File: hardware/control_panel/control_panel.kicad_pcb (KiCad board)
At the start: 2 copper layers, 70 x 37 mm, 12 parts

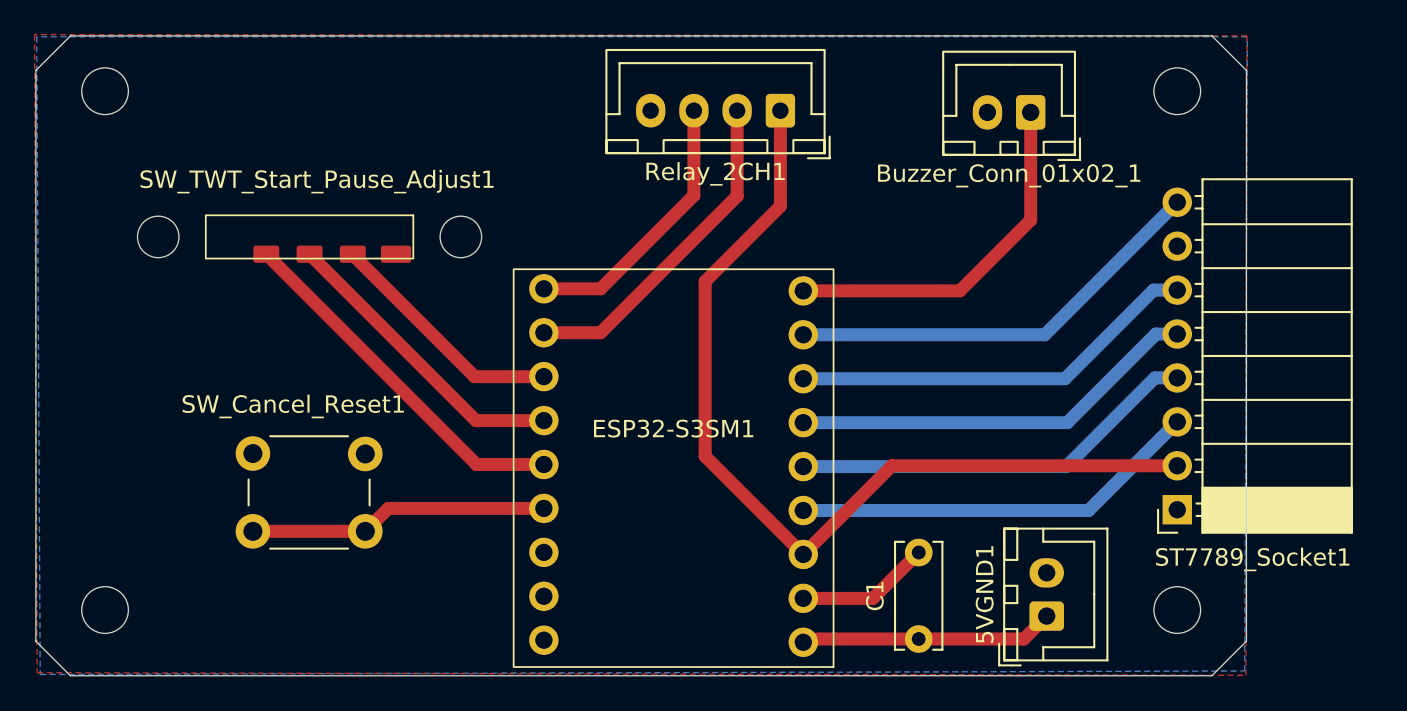
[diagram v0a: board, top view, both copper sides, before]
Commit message: KiCad changes for Control Panel PCB Mountholes
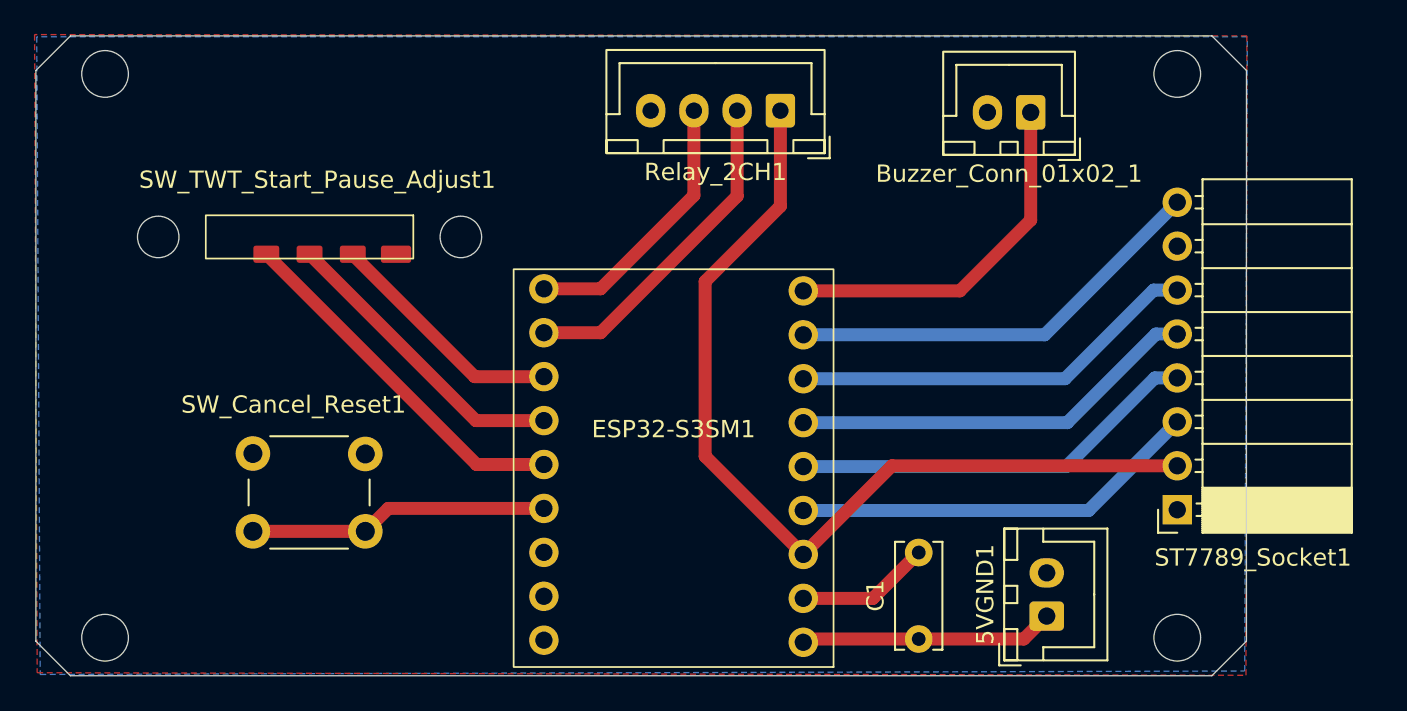
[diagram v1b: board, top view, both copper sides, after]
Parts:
- moved REF** 1.60 mm to (116.0, 84.8)
- moved REF** 1.60 mm to (54.0, 84.8)
- moved REF** 1.00 mm to (54.0, 52.2)
- moved REF** 1.00 mm to (116.0, 52.2)
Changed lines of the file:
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@@
 	(footprint "MountingHole:MountingHole_2.7mm_M2.5_DIN965"
 		(layer "F.Cu")
-		(at 116 83.2)
+		(at 116 84.8)
 		(descr "Mounting Hole 2.7mm, M2.5, no annular, generated by kicad-footprint-generator mountinghole.py")
 		(tags "mountinghole M2.5 DIN965")
@@
 	(footprint "MountingHole:MountingHole_2.7mm_M2.5_DIN965"
 		(layer "F.Cu")
-		(at 54 53.2)
+		(at 54 52.2)
 		(descr "Mounting Hole 2.7mm, M2.5, no annular, generated by kicad-footprint-generator mountinghole.py")
 		(tags "mountinghole M2.5 DIN965")
@@
 	(footprint "MountingHole:MountingHole_2.7mm_M2.5_DIN965"
 		(layer "F.Cu")
-		(at 116 53.2)
+		(at 116 52.2)
 		(descr "Mounting Hole 2.7mm, M2.5, no annular, generated by kicad-footprint-generator mountinghole.py")
 		(tags "mountinghole M2.5 DIN965")
@@
 	(footprint "MountingHole:MountingHole_2.7mm_M2.5_DIN965"
 		(layer "F.Cu")
-		(at 54 83.2)
+		(at 54 84.8)
 		(descr "Mounting Hole 2.7mm, M2.5, no annular, generated by kicad-footprint-generator mountinghole.py")
 		(tags "mountinghole M2.5 DIN965")
